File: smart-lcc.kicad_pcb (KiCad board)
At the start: 4 copper layers, 114.3 x 53.2 mm, 93 parts, among them J1 280372-1, J10 Conn_01x04_Pin, J11 USB_B_Micro, J2 F0503-ZV-20-20T-R, J3 Conn_01x24, J4 BM04B-SRSS-TB(LF)(SN), J5 BM04B-SRSS-TB(LF)(SN), J6 Micro_SD_Card_Det2, J7 F0503-ZV-20-20T-R, J8 J-Link RP2040, J9 J-Link ESP32-S3, Q1 2N7002, Q2 2N7002, SW1 SW_Push, SW2 SW_Push, SW3 SW_Push, SW4 SW_Push, SW5 SW_Push, U1 PTN04050C, U2 RP2040, U3 ESP32-S3-WROOM-1, U4 W25Q16JVSNIQ (Program Flash), U5 W25Q16JVSNIQ (Opt. Settings f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, U6 LMZ21701SILR, U7 74LVC1G125, Y1 XYDBPCNANF-12MHZ

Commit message: WIP
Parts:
- removed C25: 22uF, 25V, X5R, Capacitor_SMD:C_0805_2012Metric
- removed C26: 3300pF, 10V, X5R, Capacitor_SMD:C_0402_1005Metric
- removed C27: 22uF, 10V, X5R, Capacitor_SMD:C_0805_2012Metric
- removed J10: Conn_01x04_Pin, Connector_PinHeader_2.54mm:PinHeader_1x04_P2.54mm_Vertical
- removed J11: USB_B_Micro, Connector_USB:USB_Micro-B_Molex-105133-0001
- removed J7: F0503-ZV-20-20T-R, 2N7002:FPC_20
- removed J8: J-Link RP2040, Connector_IDC:IDC-Header_2x10_P2.54mm_Vertical
- removed J9: J-Link ESP32-S3, Connector_IDC:IDC-Header_2x10_P2.54mm_Vertical
- removed R12: 1M21, Resistor_SMD:R_0402_1005Metric
- removed R13: 383K, Resistor_SMD:R_0402_1005Metric
- removed SW3, SW4, SW5: SW_Push, SW_Push_ADTSMW65:ADTSMW65
- added Q3: 2N7002, Package_TO_SOT_SMD:SOT-23, F.Cu at (63.0, 40.8)
- added R14: 0R, Resistor_SMD:R_0402_1005Metric, F.Cu at (63.9, 69.4)
- added U8: LM5050-1, Package_TO_SOT_SMD:TSOT-23-6, F.Cu at (67.2, 41.0)
- C5, C6: value 100 uF -> NC; footprint Capacitor_THT:CP_Radial_D7.5mm_P2.50mm -> Capacitor_SMD:C_0402_1005Metric
- J1: footprint TE_280372-1:TE_280372-1 -> 280372-1:TE_280372-1
- JP1: value Jumper_2_Bridged -> SolderJumper_3_Bridged12; footprint Connector_PinHeader_2.54mm:PinHeader_1x02_P2.54mm_Vertical -> Jumper:SolderJumper-3_P1.3mm_Bridged2Bar12_RoundedPad1.0x1.5mm_NumberLabels
- R7: value 1K33, 0.01W, 1% -> 0R; footprint Resistor_THT:R_Axial_DIN0204_L3.6mm_D1.6mm_P7.62mm_Horizontal -> Resistor_SMD:R_0402_1005Metric
- U1: value PTN04050C -> MAX40200AUK; footprint Module:Texas_EUS_R-PDSS-T5_THT -> Package_TO_SOT_SMD:SOT-23-5
- U6: value LMZ21701SILR -> MAX40200AUK; footprint LMZ21701SILR:CONV_LMZ21701SILR -> Package_TO_SOT_SMD:SOT-23-5
- moved JP1 80.0 mm to (35.5, 69.2), turned to 0 degrees
- moved C6 70.3 mm to (65.5, 67.8), turned to 180 degrees
- moved U1 67.1 mm to (66.7, 50.4), turned to 180 degrees
- moved C5 59.7 mm to (63.5, 67.8), turned to 180 degrees
- moved R7 56.5 mm to (65.0, 69.4), turned to -90 degrees
- moved U6 5.01 mm to (66.7, 46.3), turned to 180 degrees
- moved TP9 4.81 mm to (69.6, 64.0)
- moved TP10 3.05 mm to (64.8, 64.2)
- moved J2 1.15 mm to (26.9, 43.6)
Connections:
- C1 pad 1: +12V -> 12V_OLED_SAFE
- C4 pad 1: +3V3 -> 3V3_OLED_SAFE
- C5 pad 1: Net-(JP1-A) -> ESP32_USB_DN
- C5 pad 2: GND2 -> GND
- C6 pad 1: 5V_DB -> GND
- C6 pad 2: GND2 -> ESP32_USB_DP
- J1 pad 1: +12V -> 12V_OLED
- J2 pad 1: +12V -> 12V_OLED_SAFE
- J2 pad 10: RP2040_ESP32_RX -> ESP32_USB_DN
- J2 pad 2: GND -> 3V3_OLED_SAFE
- J2 pad 9: RP2040_ESP32_TX -> ESP32_USB_DP
- J3 pad 23: +12V -> 12V_OLED_SAFE
- J3 pad 5: +3V3 -> 3V3_OLED_SAFE
- JP1 pad 1: Net-(JP1-A) -> GND
- JP1 pad 2: VIN_DB -> Net-(JP1-C)
- R7 pad 1: Net-(U1-Vo_Adj) -> ESP32_USB_DP
- R7 pad 2: GND2 -> /ESP32_USB_PRE_R_DP
- TP16 pad 1: +3V3 -> 3V3_OLED_SAFE
- U1 pad 1: GND2 -> 3V3_MCU
- U1 pad 2: 5V_DB -> GND
- U1 pad 3: unconnected-(U1-~{Inhibit}-Pad3) -> 3V3_MCU
- U1 pad 4: Net-(U1-Vo_Adj) -> unconnected-(U1-NC-Pad4)
- U1 pad 5: Net-(JP1-A) -> +3V3
- U3 pad 13: RP2040_ESP32_CTS -> /ESP32_USB_PRE_R_DN
- U3 pad 14: RP2040_ESP32_RTS -> /ESP32_USB_PRE_R_DP
- U3 pad 15: GND -> Net-(JP1-C)
- U3 pad 21: unconnected-(U3-GPIO13/TOUCH13/ADC2_CH2/FSPIQ/FSPIIO7/SUBSPIQ-Pad21) -> RP2040_ESP32_RTS
- U3 pad 22: unconnected-(U3-GPIO14/TOUCH14/ADC2_CH3/FSPIWP/FSPIDQS/SUBSPIWP-Pad22) -> RP2040_ESP32_CTS
- U6 pad 1: Net-(U6-SS) -> 3V3_OLED
- U6 pad 2: Net-(U6-FB) -> GND
- U6 pad 3: unconnected-(U6-PG-Pad3) -> 3V3_OLED
- U6 pad 4: +3V3 -> unconnected-(U6-NC-Pad4)
- U6 pad 5: GND -> 3V3_OLED_SAFE
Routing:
- net 5V_DB: track 117.0 -> 0.00 mm
- net 3V3_OLED_SAFE: track 0.00 -> 116.9 mm, vias 0 -> 7
- net +12V: track 95.0 -> 0.00 mm, vias 1 -> 0
- net 12V_OLED_SAFE: track 0.00 -> 84.4 mm, vias 0 -> 3
- net ESP32_USB_DN: track 0.00 -> 58.3 mm, vias 0 -> 2
- net ESP32_USB_DP: track 0.00 -> 57.1 mm, vias 0 -> 2
- net ESP32_TXD0_DB: track 56.2 -> 0.00 mm
- net GND2: track 55.0 -> 0.00 mm, vias 5 -> 0
- net ESP32_RXD0_DB: track 54.0 -> 0.00 mm
- net 3V3_DB: track 53.3 -> 0.00 mm, vias 1 -> 0
- net ESP32_EN_DB: track 50.7 -> 0.00 mm, vias 1 -> 0
- net RP2040_USB_DB_DP: track 48.0 -> 0.00 mm
- net ESP32_GPIO0_DB: track 47.9 -> 0.00 mm, vias 2 -> 0
- net RP2040_USB_DB_DN: track 46.2 -> 0.00 mm
- net ESP32_TMS_DB: track 42.0 -> 0.00 mm
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- removed copper zone on B.Cu, net GND
- removed copper zone on In2.Cu, net GND
- removed copper zone on B.Cu, net GND2
- removed copper zone on In1.Cu, net GND2
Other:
- board size 114.3 x 53.2 mm -> 53.2 x 53.2 mm
- board text added: "12V OLED"
- board text added: "3V3 MCU"
- board text added: "3V3 OLED"
- board text added: "JTAG"
- board text added: "RP B"
- board text added: "RP~R"
- board text added: "USB"
- board text removed: "12V"
- board text removed: "ESP EN"
- board text removed: "ESP GPIO0"
- board text removed: "ESP32 JTAG"
- board text removed: "ESP32 UART"
- board text removed: "Open LCC Debug board"
- board text removed: "RP Boot"
- board text removed: "RP ~Res"
- board text removed: "RP2040 Bootsel"
- board text removed: "RP2040 SWD"
- board text removed: "RP2040 USB"
- board text removed: "Supply power to LCC"

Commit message: WIP
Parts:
- J2: value F0503-ZV-20-20T-R -> F0503-ZV-24-20T-R; footprint 2N7002:FPC_20 -> 2N7002:FPC_24
- moved C8 20.9 mm to (39.9, 68.5), turned to 90 degrees
- moved TP8 4.52 mm to (33.9, 33.7)
- moved TP7 4.52 mm to (30.7, 30.5)
- moved TP3 4.38 mm to (64.8, 61.2)
- moved TP1 4.34 mm to (67.8, 61.2)
- moved TP4 4.29 mm to (64.8, 58.2)
- moved TP2 4.16 mm to (67.8, 58.3)
- moved J2 1.60 mm to (28.2, 42.7)
- moved J4 1.08 mm to (34.4, 39.2)
- moved J5 1.08 mm to (34.4, 47.9)
- moved R8 0.31 mm to (36.7, 51.6)
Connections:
- J2 pad 1: 12V_OLED_SAFE -> RP2040_USB_DP
- J2 pad 10: ESP32_USB_DN -> RP2040_RESETn
- J2 pad 2: 3V3_OLED_SAFE -> RP2040_USB_DN
- J2 pad 20: +3V3 -> GND
- J2 pad 3: RP2040_USB_DP -> 12V_OLED_SAFE
- J2 pad 4: RP2040_USB_DN -> 12V_OLED_SAFE
- J2 pad 5: RP2040_BOOTSEL -> GND
- J2 pad 6: RP2040_SWCLK -> 3V3_OLED_SAFE
- J2 pad 7: RP2040_SWD -> RP2040_BOOTSEL
- J2 pad 8: RP2040_RESETn -> RP2040_SWCLK
- J2 pad 9: ESP32_USB_DP -> RP2040_SWD
- TP1 pad 1: ESP32_EN -> ESP32_RXD0
- TP2 pad 1: ESP32_GPIO0 -> ESP32_TXD0
- TP3 pad 1: ESP32_TXD0 -> ESP32_GPIO0
- TP4 pad 1: ESP32_RXD0 -> ESP32_EN
- TP7 pad 1: RP2040_USB_DN -> RP2040_USB_DP
- TP8 pad 1: RP2040_USB_DP -> RP2040_USB_DN
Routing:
- net RP2040_QWIIC2_SDA: track 36.5 -> 26.6 mm
- net ESP32_EN: track 91.0 -> 99.7 mm
- net ESP32_TXD0: track 71.4 -> 77.2 mm
- net ESP32_USB_DP: track 57.1 -> 51.5 mm
- net ESP32_USB_DN: track 58.3 -> 52.7 mm
- net +3V3: track 235.6 -> 230.0 mm, vias 13 -> 11
- net RP2040_QWIIC2_SCL: track 32.1 -> 27.2 mm
- net ESP32_TMS: track 50.8 -> 54.2 mm
- net ESP32_TDI: track 50.7 -> 54.0 mm
- net RP2040_USB_DN: track 13.2 -> 9.94 mm
- net ESP32_GPIO0: track 52.8 -> 56.0 mm
- net RP2040_USB_DP: track 13.2 -> 10.0 mm
- net ESP32_TDO: track 55.3 -> 58.4 mm
- net ESP32_TCK: track 55.2 -> 58.3 mm
- net ESP32_RXD0: track 74.9 -> 77.1 mm
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
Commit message: R2A WIP
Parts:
- removed Q3: 2N7002, Package_TO_SOT_SMD:SOT-23
- removed TP11, TP12: TestPoint_Small, TestPoint:TestPoint_Pad_D1.0mm
- removed U1: MAX40200AUK, Package_TO_SOT_SMD:SOT-23-5
- removed U8: LM5050-1, Package_TO_SOT_SMD:TSOT-23-6
- added C25: 22 uF, 10V, X7T, Capacitor_SMD:C_0805_2012Metric, F.Cu at (63.5, 50.4)
- added C26: 5.6 nF, 50V, C0G, Capacitor_SMD:C_0402_1005Metric, F.Cu at (68.8, 47.8)
- added C27: 22 uF, 10V, X7T, Capacitor_SMD:C_0805_2012Metric, F.Cu at (63.5, 46.2)
- added C33: 10 μF, 25 V, X7R, Capacitor_SMD:C_1206_3216Metric, F.Cu at (67.0, 44.1)
- added D4: 19-217/BHC-ZL1M2RY/3T, LED_SMD:LED_0603_1608Metric, F.Cu at (69.2, 65.5)
- added D5: 19-217/BHC-ZL1M2RY/3T, LED_SMD:LED_0603_1608Metric, F.Cu at (57.5, 27.8)
- added D6: D_Schottky, Diode_SMD:D_SOD-128, F.Cu at (60.8, 43.0)
- added D7: D_Schottky, Diode_SMD:D_SOD-128, F.Cu at (66.7, 39.5)
- added J7: Conn_01x12, TFT_1.47IN_172X320_12P:TFT_1.47IN_172X320_12P, B.Cu at (49.8, 46.0)
- added J8: BM04B-SRSS-TB(LF)(SN), BM04B-SRSS-TB_LF__SN_:JST_BM04B-SRSS-TB(LF)(SN), F.Cu at (36.1, 68.1)
- added JP2: SolderJumper_3_Bridged12, Jumper:SolderJumper-3_P1.3mm_Bridged2Bar12_RoundedPad1.0x1.5mm, F.Cu at (67.2, 53.1)
- added Q4: 2N7002, Package_TO_SOT_SMD:SOT-23, F.Cu at (45.9, 46.2)
- added R12: 100R, Resistor_SMD:R_0402_1005Metric, F.Cu at (64.9, 64.9)
- added R13: 4K7, Resistor_SMD:R_0402_1005Metric, F.Cu at (37.0, 47.2)
- added R15: 4K7, Resistor_SMD:R_0402_1005Metric, F.Cu at (37.0, 46.1)
- added R16: 4K7, Resistor_SMD:R_0402_1005Metric, F.Cu at (31.8, 43.5)
- added R17: 4K7, Resistor_SMD:R_0402_1005Metric, F.Cu at (34.6, 43.5)
- added R18: 10R, Resistor_SMD:R_0402_1005Metric, F.Cu at (43.1, 47.0)
- added R19: 10K, Resistor_SMD:R_0402_1005Metric, F.Cu at (67.5, 49.5)
- added R20: 31K6, Resistor_SMD:R_0402_1005Metric, F.Cu at (65.6, 49.5)
- added R21: 10K, Resistor_SMD:R_0402_1005Metric, F.Cu at (62.7, 28.6)
- added R22: 10K, Resistor_SMD:R_0402_1005Metric, F.Cu at (70.5, 34.5)
- added R23: 100R, Resistor_SMD:R_0402_1005Metric, F.Cu at (56.3, 29.2)
- added R24: 4K7, Resistor_SMD:R_0402_1005Metric, F.Cu at (40.7, 70.5)
- added R25: 4K7, Resistor_SMD:R_0402_1005Metric, F.Cu at (37.4, 74.8)
- added TP19: TestPoint, TestPoint:TestPoint_Pad_D1.5mm, B.Cu at (59.0, 28.5)
- added TP20: TestPoint_Small, TestPoint:TestPoint_Pad_D1.5mm, B.Cu at (58.0, 53.0)
- added TP21: TestPoint_Small, TestPoint:TestPoint_Pad_D1.5mm, B.Cu at (46.0, 53.0)
- added TP22: TestPoint_Small, TestPoint:TestPoint_Pad_D1.5mm, B.Cu at (55.0, 53.0)
- added TP23: TestPoint_Small, TestPoint:TestPoint_Pad_D1.5mm, B.Cu at (49.0, 53.0)
- added TP24: TestPoint_Small, TestPoint:TestPoint_Pad_D1.5mm, B.Cu at (52.0, 53.0)
- added TP25: TestPoint_Small, TestPoint:TestPoint_Pad_D1.5mm, B.Cu at (43.0, 53.0)
- added TP26: TestPoint_Small, TestPoint:TestPoint_Pad_D1.5mm, B.Cu at (37.0, 53.0)
- added TP27: TestPoint_Small, TestPoint:TestPoint_Pad_D1.5mm, B.Cu at (40.0, 53.0)
- added TP28: TestPoint_Small, TestPoint:TestPoint_Pad_D1.0mm, F.Cu at (63.0, 65.7)
- added TP29: TestPoint_Small, TestPoint:TestPoint_Pad_D1.0mm, F.Cu at (66.3, 66.3)
- C10, C13, C14, C15, C16, C17, C18, C19, C20, C21, C22, C24, C9: value 100 nF -> 100 nF, 50V, X7R
- C28: value 22uF, 10V, X5R -> 22 uF, 10V, X5R; footprint Capacitor_SMD:C_0805_2012Metric -> Capacitor_SMD:C_0603_1608Metric
- JP1: moved to B.Cu
- R2, R3: value 20R -> 100R
- TP13: value TestPoint_Small -> TestPoint
- TP14, TP15, TP16: value TestPoint_Small -> TestPoint; footprint TestPoint:TestPoint_Pad_D1.0mm -> TestPoint:TestPoint_Pad_D1.5mm; moved to B.Cu
- U6: value MAX40200AUK -> TPS82130; footprint Package_TO_SOT_SMD:SOT-23-5 -> Package_LGA:Texas_SIL0008D_MicroSiP-8-1EP_2.8x3mm_P0.65mm_EP1.1x1.9mm_ThermalVias
- moved TP13 30.4 mm to (73.7, 62.8)
- moved TP5 24.4 mm to (49.6, 46.3)
- moved TP6 24.2 mm to (51.8, 46.3)
- moved TP9 23.7 mm to (53.9, 46.3)
- moved TP10 19.9 mm to (56.0, 46.3)
- moved TP14 18.8 mm to (39.5, 28.5), turned to 180 degrees
- moved TP16 18.3 mm to (52.5, 28.5), turned to 180 degrees
- moved TP15 18.3 mm to (46.0, 28.5), turned to 180 degrees
- moved TP4 8.21 mm to (71.5, 62.8)
- moved JP1 7.32 mm to (32.5, 62.5), turned to 180 degrees
- moved TP2 5.19 mm to (65.2, 62.8)
- moved TP3 4.94 mm to (69.5, 62.8)
- moved TP18 4.51 mm to (65.2, 59.3)
- moved TP17 4.49 mm to (67.3, 59.3)
- moved TP1 1.65 mm to (67.3, 62.8)
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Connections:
- C1 pad 1: 12V_OLED_SAFE -> VIN
- C4 pad 1: 3V3_OLED_SAFE -> +3V3
- J2 pad 3: 12V_OLED_SAFE -> Net-(D6-A)
- J2 pad 4: 12V_OLED_SAFE -> Net-(D6-A)
- J2 pad 6: 3V3_OLED_SAFE -> unconnected-(J2-Pin_6-Pad6)
- J3 pad 23: 12V_OLED_SAFE -> VIN
- J3 pad 5: 3V3_OLED_SAFE -> +3V3
- SW1 pad 2: SW_MINUS -> SW_PLUS
- SW2 pad 2: SW_PLUS -> SW_MINUS
- TP13 pad 1: SSD1309_DC -> Net-(U3-GPIO7/TOUCH7/ADC1_CH6)
- TP14 pad 1: SSD1309_RES -> Net-(U2-GPIO26_ADC0)
- TP15 pad 1: SSD1309_CS -> Net-(U2-GPIO27_ADC1)
- TP16 pad 1: 3V3_OLED_SAFE -> Net-(U2-GPIO28_ADC2)
- U2 pad 16: RP2040_SET_CS -> RP2040_SET_D2
- U2 pad 17: RP2040_SD_DET_A -> RP2040_SET_D3
- U2 pad 18: RP2040_SD_DET_B -> RP2040_SD_DET_A
- U2 pad 27: RP2040_SERIAL_BOOT -> RP2040_SD_DET_B
- U2 pad 28: unconnected-(U2-GPIO17-Pad28) -> RP2040_SET_CS
- U2 pad 36: unconnected-(U2-GPIO24-Pad36) -> RP2040_SERIAL_BOOT
- U2 pad 37: unconnected-(U2-GPIO25-Pad37) -> Net-(U2-GPIO25)
- U2 pad 38: unconnected-(U2-GPIO26_ADC0-Pad38) -> Net-(U2-GPIO26_ADC0)
- U2 pad 39: unconnected-(U2-GPIO27_ADC1-Pad39) -> Net-(U2-GPIO27_ADC1)
- U2 pad 40: unconnected-(U2-GPIO28_ADC2-Pad40) -> Net-(U2-GPIO28_ADC2)
- U2 pad 41: unconnected-(U2-GPIO29_ADC3-Pad41) -> Net-(U2-GPIO29_ADC3)
- U3 pad 23: SW_PLUS -> SW_MINUS
- U3 pad 24: unconnected-(U3-GPIO47/SPICLK_P/SUBSPICLK_P_DIFF-Pad24) -> BACKLIGHT
- U3 pad 25: unconnected-(U3-GPIO48/SPICLK_N/SUBSPICLK_N_DIFF-Pad25) -> Net-(U3-GPIO48/SPICLK_N/SUBSPICLK_N_DIFF)
- U3 pad 31: SW_MINUS -> SW_PLUS
- U3 pad 38: unconnected-(U3-GPIO2/TOUCH2/ADC1_CH1-Pad38) -> ESP32_QWIIC_SDA
- U3 pad 39: unconnected-(U3-GPIO1/TOUCH1/ADC1_CH0-Pad39) -> ESP32_QWIIC_SCL
- U3 pad 7: unconnected-(U3-GPIO7/TOUCH7/ADC1_CH6-Pad7) -> Net-(U3-GPIO7/TOUCH7/ADC1_CH6)
- U5 pad 3: unconnected-(U5-~{WP}/IO2-Pad3) -> RP2040_SET_D3
- U5 pad 7: unconnected-(U5-~{HOLD}/IO3-Pad7) -> RP2040_SET_D2
- U6 pad 1: 3V3_OLED -> VIN
- U6 pad 2: GND -> VIN
- U6 pad 3: 3V3_OLED -> GND
- U6 pad 4: unconnected-(U6-NC-Pad4) -> 3V3_OUT
- U6 pad 5: 3V3_OLED_SAFE -> 3V3_OUT
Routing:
- net 3V3_OLED_SAFE: track 116.4 -> 0.00 mm, vias 7 -> 0
- net 12V_OLED_SAFE: track 86.5 -> 0.00 mm, vias 3 -> 0
- net +3V3: track 230.0 -> 300.1 mm, vias 11 -> 16
- net Net-(D6-A): track 0.00 -> 59.0 mm, vias 0 -> 3
- net BACKLIGHT: track 0.00 -> 49.0 mm, vias 0 -> 2
- net GND: track 137.6 -> 169.1 mm, vias 73 -> 84
- net Net-(U3-GPIO7/TOUCH7/ADC1_CH6): track 0.00 -> 30.3 mm, vias 0 -> 2
- net RP2040_RESETn: track 100.2 -> 71.4 mm, vias 5 -> 7
- net Net-(U2-GPIO26_ADC0): track 0.00 -> 24.9 mm, vias 0 -> 1
- net VIN: track 0.00 -> 24.5 mm
- net ESP32_QWIIC_SDA: track 0.00 -> 24.1 mm, vias 0 -> 2
- net ESP32_QWIIC_SCL: track 0.00 -> 22.4 mm, vias 0 -> 2
- net RP2040_SET_D2: track 0.00 -> 19.3 mm, vias 0 -> 3
- net RP2040_ESP32_RX: track 70.9 -> 52.8 mm
- net SSD1309_DC: track 32.4 -> 48.9 mm, vias 0 -> 2
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- added copper zone on F.Cu, net 3V3_OUT
- added copper zone on B.Cu, net GND
- added copper zone on F.Cu, net GND
- added copper zone on F.Cu, net VIN
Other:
- board text added: "1"
- board text added: "12"
- board text added: "12V"
- board text added: "3V3 Power"
- board text added: "BL"
- board text added: "Boot"
- board text added: "Bus"
- board text added: "CK"
- board text added: "DBG"
- board text added: "ESP32-S3"
- board text added: "GP25"
- board text added: "GP26"
- board text added: "GP27"
- board text added: "GP28"
- board text added: "GP29"
- board text added: "GP48"
- board text added: "GP7"
- board text added: "On Board"
- board text added: "RES"
- board text added: "RP2040"
- board text added: "RP2040 GPIO"
- board text added: "Rev R2A"
- board text added: "~R"
- board text removed: "12V OLED"
- board text removed: "CLK"
- board text removed: "ESP -> RP"
- board text removed: "RP -> ESP"
- board text removed: "RP B"
- board text removed: "RP~R"
- board text removed: "Res"
- board text removed: "Rev A"

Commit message: Initial work on R2B
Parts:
- removed D6, D7: D_Schottky, Diode_SMD:D_SOD-128
- added Q3: 2N7002, Package_TO_SOT_SMD:SOT-23, F.Cu at (62.0, 44.0)
- added Q5: 2N7002, Package_TO_SOT_SMD:SOT-23, F.Cu at (67.3, 44.0)
- added U1: LM5050-1, Package_TO_SOT_SMD:TSOT-23-6, F.Cu at (67.3, 39.9)
- added U8: LM5050-1, Package_TO_SOT_SMD:TSOT-23-6, F.Cu at (61.9, 39.9)
- moved JP2 7.77 mm to (73.1, 58.2)
- moved C25 4.05 mm to (63.3, 54.5)
- moved C26 4.05 mm to (68.6, 51.9)
- moved U6 4.05 mm to (66.2, 51.2)
- moved C27 4.05 mm to (63.3, 50.2)
- moved C33 4.05 mm to (66.8, 48.1)
- moved R19 4.05 mm to (67.3, 53.5)
- moved R20 4.05 mm to (65.4, 53.5)
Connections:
- net Net-(D6-A) renamed VIN_DEBUG
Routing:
- net 12V_OLED: track 4.31 -> 12.9 mm
- net Net-(Q3-G): track 0.00 -> 6.22 mm, vias 0 -> 2
- net VIN: track 24.5 -> 30.5 mm
- net 3V3_OUT: track 3.02 -> 9.01 mm
- net +3V3: track 300.1 -> 294.2 mm, vias 16 -> 20
- net Net-(Q5-G): track 0.00 -> 5.91 mm, vias 0 -> 2
- net VIN_DEBUG: track 59.0 -> 63.4 mm
- net GND: track 169.1 -> 172.9 mm, vias 84 -> 86
- net 3V3_MCU: track 5.09 -> 6.91 mm
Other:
- board text added: "Rev R2B"
- board text removed: "Rev R2A"

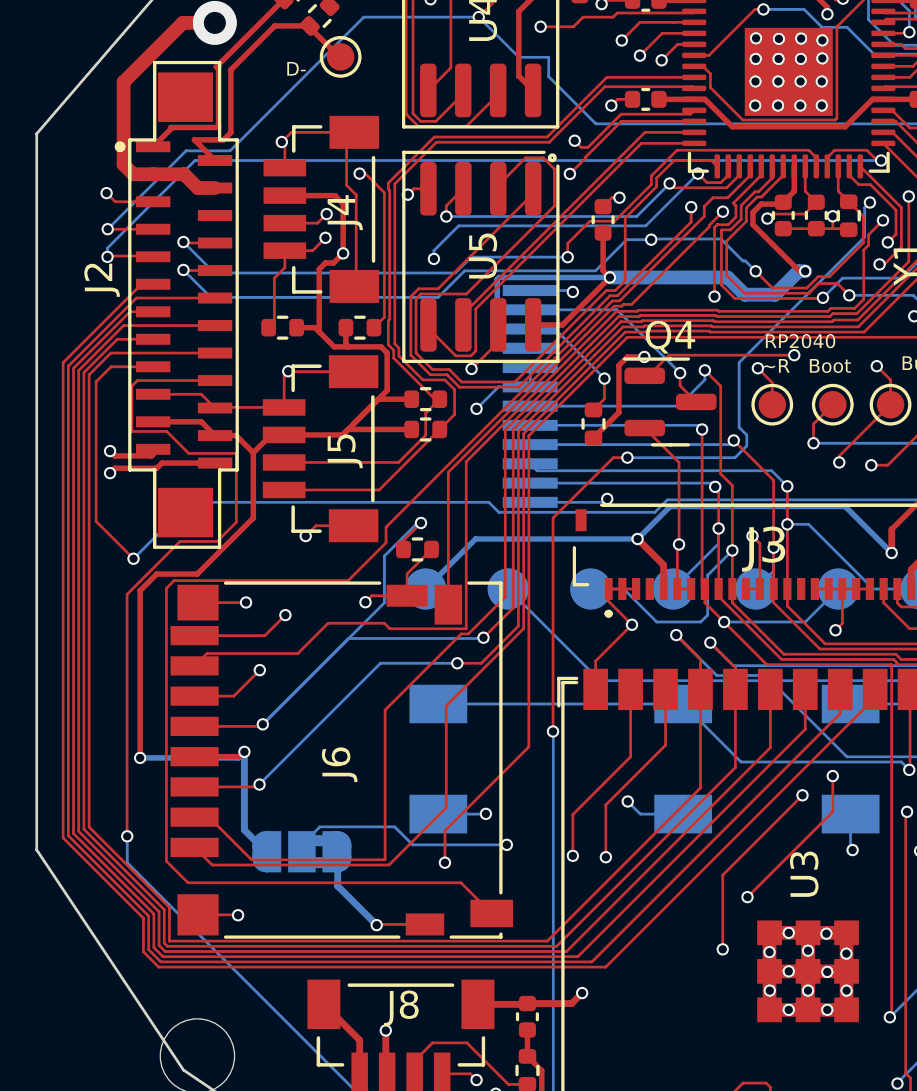
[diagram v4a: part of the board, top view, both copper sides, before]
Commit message: Removed SD_DET_A from RP2040 and connected DET_A on the SD card to GND
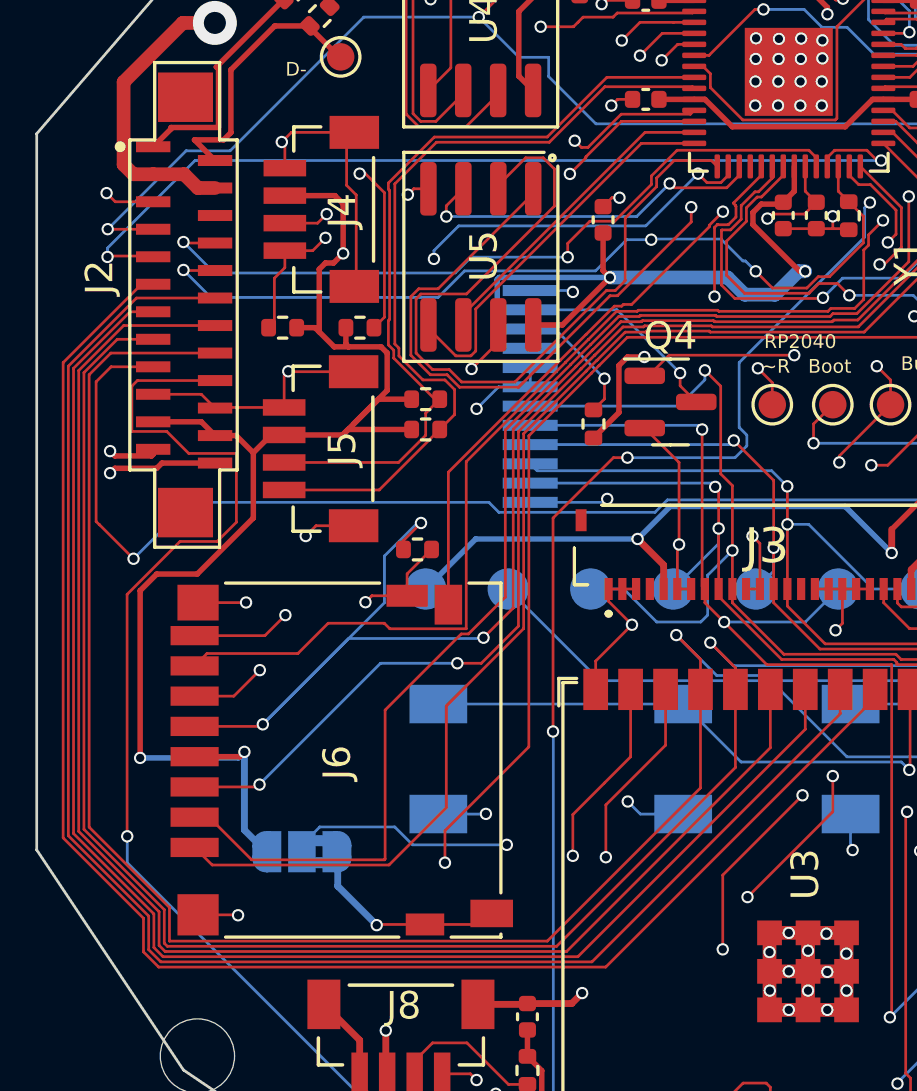
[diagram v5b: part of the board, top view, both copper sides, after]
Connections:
- J6 pad 10: RP2040_SD_DET_A -> GND
- U2 pad 18: RP2040_SD_DET_A -> unconnected-(U2-GPIO15-Pad18)
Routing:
- net RP2040_SD_DET_A: track 50.8 -> 0.00 mm
- net GND: track 172.9 -> 175.5 mm
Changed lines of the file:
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@@
   (net 74 "RP2040_SD_MISO_DAT0")
   (net 75 "RP2040_SD_DET_B")
-  (net 76 "RP2040_SD_DET_A")
+  (net 76 "unconnected-(U2-GPIO15-Pad18)")
   (net 77 "VIN")
   (net 78 "+3V3")
@@
       (net 75 "RP2040_SD_DET_B") (pinfunction "DET_B") (pintype "passive"))
     (pad "10" smd rect (at 5.575 -5.45 270) (size 1 1.55) (layers "F.Cu" "F.Paste" "F.Mask")
-      (net 76 "RP2040_SD_DET_A") (pinfunction "DET_A") (pintype "passive"))
+      (net 2 "GND") (pinfunction "DET_A") (pintype "passive"))
     (pad "11" smd rect (at -5.975 -2.375 270) (size 0.8 1.5) (layers "F.Cu" "F.Paste" "F.Mask")
       (net 2 "GND") (pinfunction "SHIELD") (pintype "passive"))
@@
       (net 68 "RP2040_SET_D3") (pinfunction "GPIO14") (pintype "bidirectional"))
     (pad "18" smd roundrect (at -1.4 3.4375) (size 0.2 0.875) (layers "F.Cu" "F.Paste" "F.Mask") (roundrect_rratio 0.25)
-      (net 76 "RP2040_SD_DET_A") (pinfunction "GPIO15") (pintype "bidirectional"))
+      (net 76 "unconnected-(U2-GPIO15-Pad18)") (pinfunction "GPIO15") (pintype "bidirectional+no_connect"))
     (pad "19" smd roundrect (at -1 3.4375) (size 0.2 0.875) (layers "F.Cu" "F.Paste" "F.Mask") (roundrect_rratio 0.25)
       (net 2 "GND") (pinfunction "TESTEN") (pintype "input"))
@@
   (segment (start 55.15 53) (end 56.77 53) (width 0.1) (layer "F.Cu") (net 2))
   (segment (start 36.325 52.45) (end 36.325 53.245) (width 0.1) (layer "F.Cu") (net 2))
+  (segment (start 39 65.195) (end 39.4 64.795) (width 0.1) (layer "F.Cu") (net 2))
   (segment (start 40.02 74.05) (end 41.61 74.05) (width 0.1) (layer "F.Cu") (net 2))
   (segment (start 49.15 53) (end 48.65 53) (width 0.1) (layer "F.Cu") (net 2))
   (segment (start 43.18 56.65) (end 43.18 55.62) (width 0.1) (layer "F.Cu") (net 2))
+  (segment (start 36.975 65.195) (end 39 65.195) (width 0.1) (layer "F.Cu") (net 2))
   (segment (start 48.002951 39.756867) (end 47.609447 39.756867) (width 0.1) (layer "F.Cu") (net 2))
   (segment (start 28.725 53.495) (end 30.465 53.495) (width 0.1) (layer "F.Cu") (net 2))
@@
   (segment (start 47.806199 39.281867) (end 48.924332 40.4) (width 0.1) (layer "In2.Cu") (net 75))
   (segment (start 48.924332 40.4) (end 53.8 40.4) (width 0.1) (layer "In2.Cu") (net 75))
-  (segment (start 27.575 62.895) (end 27.575 52.976432) (width 0.1) (layer "F.Cu") (net 76))
-  (segment (start 41.702697 44.608053) (end 41.702698 44.605794) (width 0.1) (layer "F.Cu") (net 76))
-  (segment (start 35.56 50.75075) (end 41.702697 44.608053) (width 0.1) (layer "F.Cu") (net 76))
-  (segment (start 39.4 64.795) (end 38.285 63.68) (width 0.1) (layer "F.Cu") (net 76))
-  (segment (start 35.56 51.3205) (end 35.56 50.75075) (width 0.1) (layer "F.Cu") (net 76))
-  (segment (start 48.8 37.957843) (end 48.8 37.6375) (width 0.1) (layer "F.Cu") (net 76))
-  (segment (start 27.856432 52.695) (end 34.1855 52.695) (width 0.1) (layer "F.Cu") (net 76))
-  (segment (start 47.128595 39.092716) (end 47.443511 38.7778) (width 0.1) (layer "F.Cu") (net 76))
-  (segment (start 42.757793 43.552957) (end 43.78305 42.5277) (width 0.1) (layer "F.Cu") (net 76))
-  (segment (start 28.36 63.68) (end 27.575 62.895) (width 0.1) (layer "F.Cu") (net 76))
-  (segment (start 34.1855 52.695) (end 35.56 51.3205) (width 0.1) (layer "F.Cu") (net 76))
-  (segment (start 47.980043 38.7778) (end 48.8 37.957843) (width 0.1) (layer "F.Cu") (net 76))
-  (segment (start 42.755534 43.552957) (end 42.757793 43.552957) (width 0.1) (layer "F.Cu") (net 76))
-  (segment (start 27.575 52.976432) (end 27.856432 52.695) (width 0.1) (layer "F.Cu") (net 76))
-  (segment (start 47.443511 38.7778) (end 47.980043 38.7778) (width 0.1) (layer "F.Cu") (net 76))
-  (segment (start 38.285 63.68) (end 28.36 63.68) (width 0.1) (layer "F.Cu") (net 76))
-  (segment (start 41.702698 44.605794) (end 42.755534 43.552957) (width 0.1) (layer "F.Cu") (net 76))
-  (segment (start 44.050191 42.5277) (end 47.128595 39.449296) (width 0.1) (layer "F.Cu") (net 76))
-  (segment (start 43.78305 42.5277) (end 44.050191 42.5277) (width 0.1) (layer "F.Cu") (net 76))
-  (segment (start 47.128595 39.449296) (end 47.128595 39.092716) (width 0.1) (layer "F.Cu") (net 76))
   (segment (start 61.9625 44.8875) (end 67.3 44.8875) (width 0.5) (layer "F.Cu") (net 77))
   (segment (start 61.9625 44.8875) (end 61.9625 40.85) (width 0.5) (layer "F.Cu") (net 77))
